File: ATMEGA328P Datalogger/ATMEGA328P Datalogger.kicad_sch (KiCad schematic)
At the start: 25 parts, among them U1 ATMEGA328P-AU, U2 24LC1025, U3 24LC1025, U4 DS1337S_, Y1 Crystal, Y2 Crystal

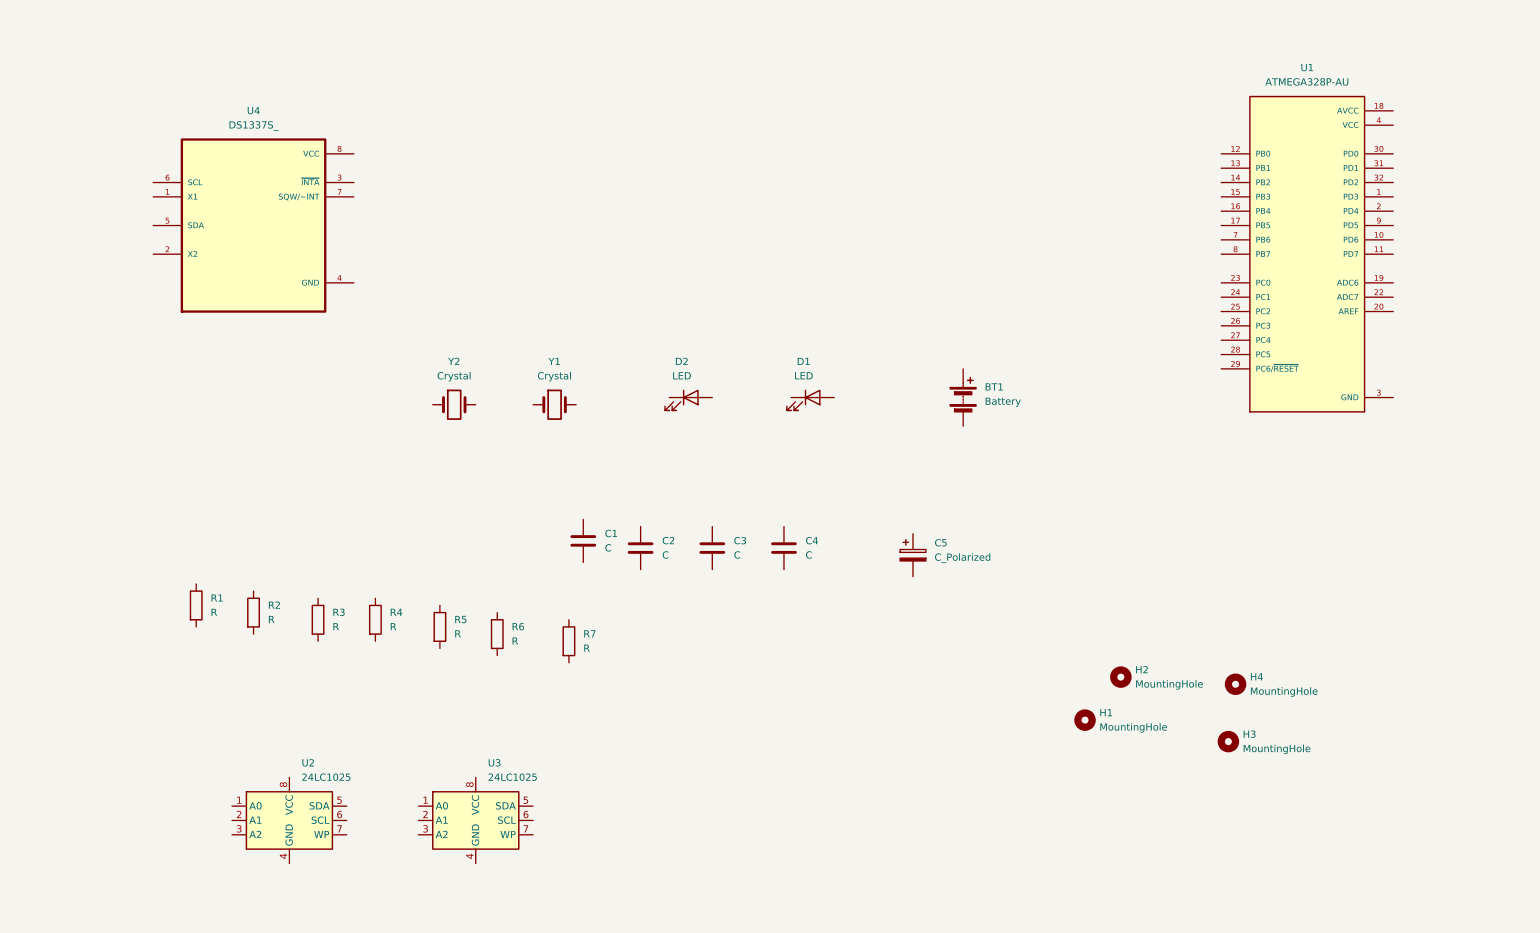
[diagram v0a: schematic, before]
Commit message: component value has been added.
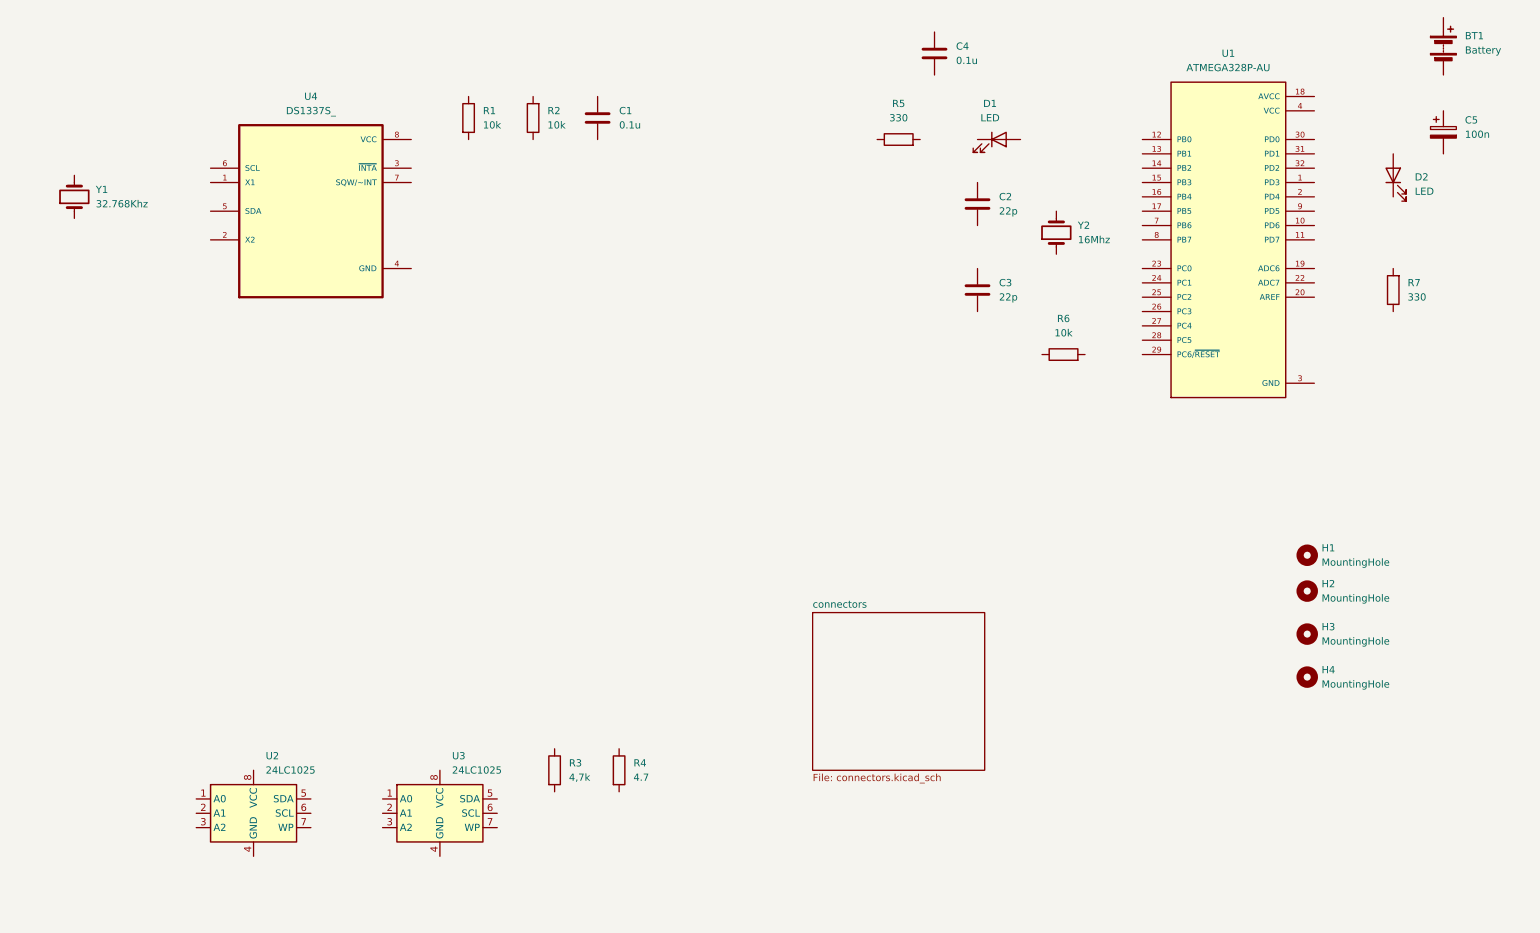
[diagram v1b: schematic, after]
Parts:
- C1, C4: value C -> 0.1u
- C2, C3: value C -> 22p
- C5: value C_Polarized -> 100n
- R1, R2, R6: value R -> 10k
- R3: value R -> 4,7k
- R4: value R -> 4.7
- R5, R7: value R -> 330
- Y1: value Crystal -> 32.768Khz
- Y2: value Crystal -> 16Mhz
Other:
- added sheet connectors (connectors.kicad_sch)
- moved on the sheet: BT1, C1, C2, C3, C4, C5, D1, D2, H1, H2, H3, H4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

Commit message: footprints assigned
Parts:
- BT1: footprint (none) -> Connector_PinSocket_2.54mm:PinSocket_1x02_P2.54mm_Vertical
- C1, C2, C3, C4, C5: footprint (none) -> Capacitor_SMD:C_0805_2012Metric
- D1, D2: footprint (none) -> LED_SMD:LED_0805_2012Metric
- H1, H2, H3, H4: footprint (none) -> MountingHole:MountingHole_2.1mm
- R1, R2, R3, R4, R5, R6, R7: footprint (none) -> Resistor_SMD:R_0805_2012Metric
- U2, U3: footprint (none) -> Package_SO:SOIC-8_5.3x5.3mm_P1.27mm
- Y1, Y2: footprint (none) -> Crystal:Crystal_SMD_5032-2Pin_5.0x3.2mm_HandSoldering
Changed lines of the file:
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@@
 			)
 		)
-		(property "Footprint" ""
+		(property "Footprint" "MountingHole:MountingHole_2.1mm"
 			(at 246.38 123.19 0)
 			(hide yes)
@@
 			)
 		)
-		(property "Footprint" ""
+		(property "Footprint" "MountingHole:MountingHole_2.1mm"
 			(at 246.38 129.54 0)
 			(hide yes)
@@
 			)
 		)
-		(property "Footprint" ""
+		(property "Footprint" "Capacitor_SMD:C_0805_2012Metric"
 			(at 181.3052 38.1 0)
 			(hide yes)
@@
 			)
 		)
-		(property "Footprint" ""
+		(property "Footprint" "Package_SO:SOIC-8_5.3x5.3mm_P1.27mm"
 			(at 59.69 168.91 0)
 			(hide yes)
@@
 			)
 		)
-		(property "Footprint" ""
+		(property "Footprint" "Resistor_SMD:R_0805_2012Metric"
 			(at 173.99 51.308 90)
 			(hide yes)
@@
 			)
 		)
-		(property "Footprint" ""
+		(property "Footprint" "Package_SO:SOIC-8_5.3x5.3mm_P1.27mm"
 			(at 92.71 168.91 0)
 			(hide yes)
@@
 			)
 		)
-		(property "Footprint" ""
+		(property "Footprint" "Resistor_SMD:R_0805_2012Metric"
 			(at 96.012 45.72 90)
 			(hide yes)
@@
 			)
 		)
-		(property "Footprint" ""
+		(property "Footprint" "Resistor_SMD:R_0805_2012Metric"
 			(at 203.2 89.408 90)
 			(hide yes)
@@
 			)
 		)
-		(property "Footprint" ""
+		(property "Footprint" "LED_SMD:LED_0805_2012Metric"
 			(at 261.62 55.88 0)
 			(hide yes)
@@
 			)
 		)
-		(property "Footprint" ""
+		(property "Footprint" "Resistor_SMD:R_0805_2012Metric"
 			(at 263.398 76.2 90)
 			(hide yes)
@@
 			)
 		)
-		(property "Footprint" ""
+		(property "Footprint" "LED_SMD:LED_0805_2012Metric"
 			(at 191.77 49.53 0)
 			(hide yes)
@@
 			)
 		)
-		(property "Footprint" ""
+		(property "Footprint" "Crystal:Crystal_SMD_5032-2Pin_5.0x3.2mm_HandSoldering"
 			(at 27.94 59.69 0)
 			(hide yes)
@@
 			)
 		)
-		(property "Footprint" ""
+		(property "Footprint" "MountingHole:MountingHole_2.1mm"
 			(at 246.38 137.16 0)
 			(hide yes)
@@
 			)
 		)
-		(property "Footprint" ""
+		(property "Footprint" "Resistor_SMD:R_0805_2012Metric"
 			(at 111.252 161.29 90)
 			(hide yes)
@@
 			)
 		)
-		(property "Footprint" ""
+		(property "Footprint" "Capacitor_SMD:C_0805_2012Metric"
 			(at 188.9252 80.01 0)
 			(hide yes)
@@
 			)
 		)
-		(property "Footprint" ""
+		(property "Footprint" "Capacitor_SMD:C_0805_2012Metric"
 			(at 271.4752 52.07 0)
 			(hide yes)
@@
 			)
 		)
-		(property "Footprint" ""
+		(property "Footprint" "Resistor_SMD:R_0805_2012Metric"
 			(at 122.682 161.29 90)
 			(hide yes)
@@
 			)
 		)
-		(property "Footprint" ""
+		(property "Footprint" "Resistor_SMD:R_0805_2012Metric"
 			(at 110.998 45.72 90)
 			(hide yes)
@@
 			)
 		)
-		(property "Footprint" ""
+		(property "Footprint" "Crystal:Crystal_SMD_5032-2Pin_5.0x3.2mm_HandSoldering"
 			(at 201.93 66.04 0)
 			(hide yes)
@@
 			)
 		)
-		(property "Footprint" ""
+		(property "Footprint" "Capacitor_SMD:C_0805_2012Metric"
 			(at 121.6152 49.53 0)
 			(hide yes)
@@
 			)
 		)
-		(property "Footprint" ""
+		(property "Footprint" "MountingHole:MountingHole_2.1mm"
 			(at 246.38 144.78 0)
 			(hide yes)
@@
 			)
 		)
-		(property "Footprint" ""
+		(property "Footprint" "Connector_PinSocket_2.54mm:PinSocket_1x02_P2.54mm_Vertical"
 			(at 270.51 31.496 90)
 			(hide yes)
@@
 			)
 		)
-		(property "Footprint" ""
+		(property "Footprint" "Capacitor_SMD:C_0805_2012Metric"
 			(at 188.9252 64.77 0)
 			(hide yes)

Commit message: do next things tomorrow
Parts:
- R3: value 4,7k -> 4.7k; Purpose (none) -> PULL_UP resistor
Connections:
- net GND: now also BT1.2 (-), C1.2, C5.2, R7.1, U2.4 (GND), U2.7 (WP), U3.2 (A1), U3.4 (GND), U3.7 (WP), U4.4 (GND)
- net VCC: now also C1.1, R1.1, R2.2, R3.1, R4.1, U2.1 (A0), U2.2 (A1), U2.3 (A2), U2.8 (VCC), U3.1 (A0), U3.3 (A2), U3.8 (VCC), U4.8 (VCC)
- net at U1.18 (AVCC): now also BT1.1 (+), C5.1, D2.2 (A)
- net SDA: now reaches U2.5 (SDA)
- net SDA: now also R4.2, U3.5 (SDA), U4.5 (SDA)
- net SCL: now reaches U2.6 (SCL)
- net SCL: now also R3.2, U3.6 (SCL), U4.6 (SCL)
- net at R1.2: now also U4.3 (~{INTA})
- net at D2.1 (K): now also R7.2
- net at Y1.1: now also U4.2 (X2)
- net at Y1.2: now also U4.1 (X1)
- net at U4.7 (SQW/~INT): now also R2.1
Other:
- moved on the sheet: BT1, C1, C5, D2, R1, R2, R7, U4, Y1

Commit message: Finally all bugs settled
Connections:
- net GND: now also C2.1, C3.1, C4.2, R5.1
- net SCL: now also D1.2 (A), U1.17 (PB5), U1.28 (PC5)
- net SDA: now also U1.27 (PC4)
- net VCC: now also BT1.1 (+), C5.1, D2.2 (A), R6.1, U1.18 (AVCC)
- net D3: now reaches U1.1 (PD3)
- net D6: now reaches U1.10 (PD6)
- net D7: now reaches U1.11 (PD7)
- net D8: now reaches U1.12 (PB0)
- net MISO: now reaches U1.15 (PB3)
- net MOSI: now reaches U1.16 (PB4)
- net D4: now reaches U1.2 (PD4)
- net at U1.20 (AREF): now also C4.1
- net RESET: now reaches U1.29 (PC6/~{RESET})
- net RESET: now also R6.2
- net RX: now reaches U1.30 (PD0)
- net TX: now reaches U1.31 (PD1)
- net D2: now reaches U1.32 (PD2)
- net at U1.7 (PB6): now also C2.2, Y2.2
- net at U1.8 (PB7): now also C3.2, Y2.1
- net D5: now reaches U1.9 (PD5)
- net at R5.2: now also D1.1 (K)
- no-connect marks 0 -> 8
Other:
- sheet connectors: file connectors.kicad_sch -> connection new.kicad_sch
- sheet connectors ports: added D2, D3, D4, D5, D6, D7, D8, GND, MISO, MOSI, RESET, RX, SCL, SDA, TX, VCC; removed none
- moved on the sheet: C2, C3, D1, R5, R6, Y2
